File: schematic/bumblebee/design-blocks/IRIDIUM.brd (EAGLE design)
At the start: 3 parts

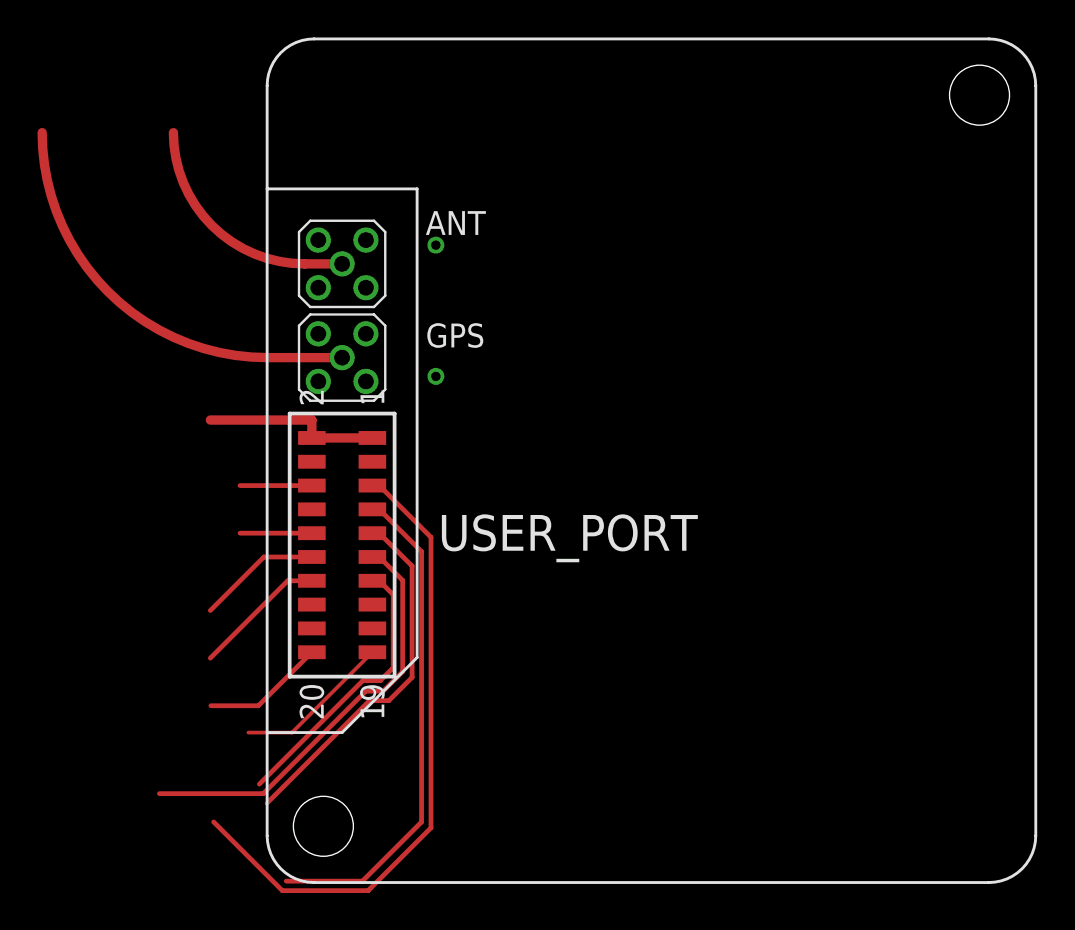
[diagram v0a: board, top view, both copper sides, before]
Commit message: Добавлена библиотека с разьёмами для игла Design-block иридиума Вроде готовая схема ICU, но её нужно проверить и причесать
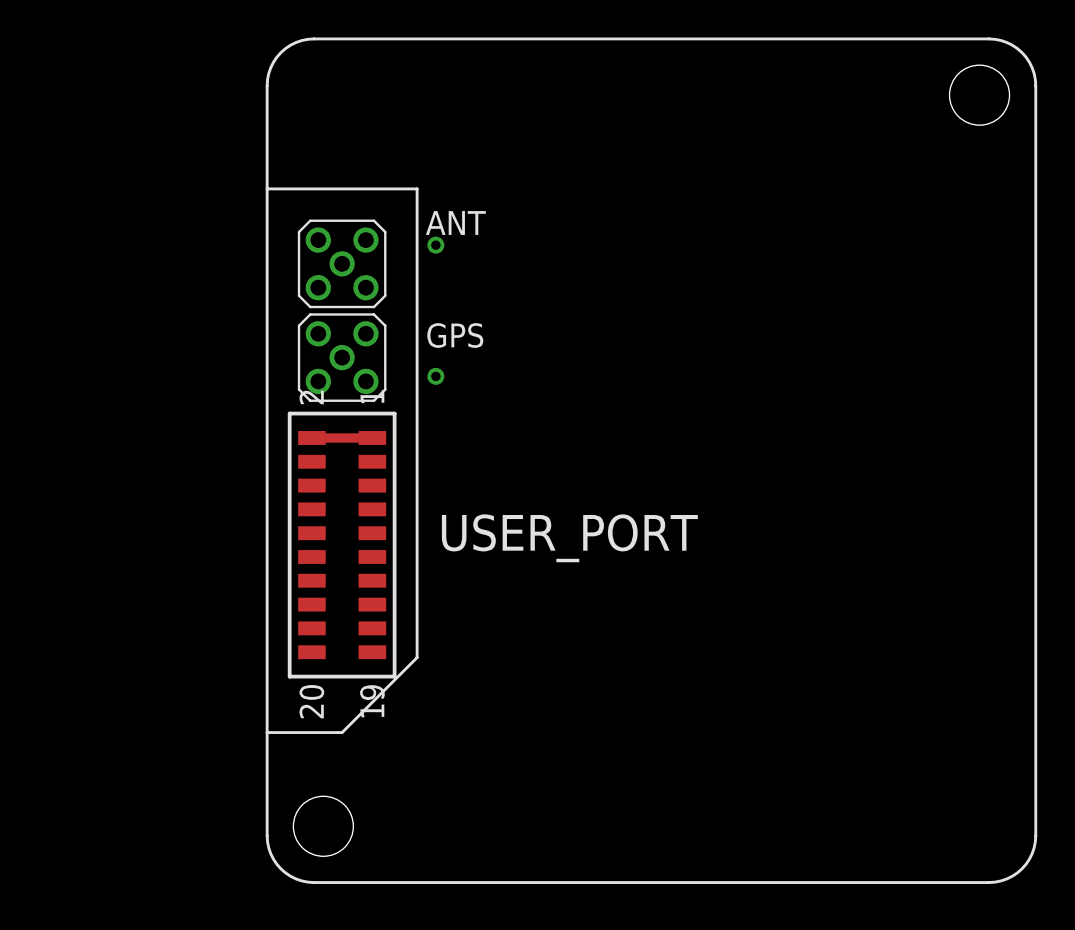
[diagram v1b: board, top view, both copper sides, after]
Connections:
- net DF_CTS renamed S$4
- net DF_DCD renamed S$3
- net DF_RTS renamed S$5
- net DF_S_RX renamed S$1
- net ON_OFF renamed S$2
- removed net DF_DSR: USER_PORT.10
- removed net DF_DTR: USER_PORT.14
- removed net DF_RI: USER_PORT.12
- removed net DF_S_TX: USER_PORT.6
- removed net N$21: ANT.1
- removed net N$22: GPS.1
- removed net NETWORK_AVAILABLE: USER_PORT.19
- removed net SUPPLY_OUT: USER_PORT.20
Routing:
- net S$2: track 34.3 -> 0.32 mm
- net S$1: track 26.5 -> 0.40 mm
- net S$4: track 22.7 -> 0.40 mm
- net N$22: track 21.0 -> 0.00 mm
- net S$3: track 19.4 -> 0.32 mm
- net S$5: track 15.0 -> 0.40 mm
- net N$21: track 11.9 -> 0.00 mm
- net NETWORK_AVAILABLE: track 8.39 -> 0.00 mm
- net DF_DTR: track 7.13 -> 0.00 mm
- net DF_RI: track 6.60 -> 0.00 mm
- net SUPPLY_OUT: track 6.57 -> 0.00 mm
- net VCC5: track 9.60 -> 3.23 mm
- net DF_S_TX: track 3.83 -> 0.00 mm
- net DF_DSR: track 3.83 -> 0.00 mm
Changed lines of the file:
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@@
 <via x="37.43" y="55.78" extent="1-16" drill="0.5"/>
-</signal>
-<signal name="NETWORK_AVAILABLE">
-<contactref element="USER_PORT" pad="19"/>
-<wire x1="34.043" y1="34.065" x2="29.758" y2="29.78" width="0.2" layer="1"/>
-<wire x1="29.758" y1="29.78" x2="27.43" y2="29.78" width="0.2" layer="1"/>
-</signal>
-<signal name="SUPPLY_OUT">
-<contactref element="USER_PORT" pad="20"/>
-<wire x1="30.817" y1="34.065" x2="27.962" y2="31.21" width="0.254" layer="1"/>
-<wire x1="27.962" y1="31.21" x2="25.43" y2="31.21" width="0.254" layer="1"/>
 </signal>
 <signal name="RESERVED_1">
 <contactref element="USER_PORT" pad="16"/>
 </signal>
-<signal name="DF_DTR">
-<contactref element="USER_PORT" pad="14"/>
-<wire x1="30.817" y1="37.875" x2="29.525" y2="37.875" width="0.254" layer="1"/>
-<wire x1="29.525" y1="37.875" x2="25.4" y2="33.75" width="0.254" layer="1"/>
-</signal>
-<signal name="DF_RI">
-<contactref element="USER_PORT" pad="12"/>
-<wire x1="30.817" y1="39.145" x2="28.255" y2="39.145" width="0.254" layer="1"/>
-<wire x1="28.255" y1="39.145" x2="25.4" y2="36.29" width="0.254" layer="1"/>
-</signal>
-<signal name="DF_DSR">
-<contactref element="USER_PORT" pad="10"/>
-<wire x1="30.817" y1="40.415" x2="26.985" y2="40.415" width="0.254" layer="1"/>
-</signal>
-<signal name="DF_S_TX">
-<contactref element="USER_PORT" pad="6"/>
-<wire x1="30.817" y1="42.955" x2="26.985" y2="42.955" width="0.254" layer="1"/>
-</signal>
 <signal name="RESERVED_2\">
 <contactref element="USER_PORT" pad="17"/>
 </signal>
-<signal name="DF_RTS">
+<signal name="S$5">
 <contactref element="USER_PORT" pad="13"/>
-<wire x1="34.43415625" y1="37.852" x2="35.155" y2="37.13115625" width="0.254" layer="1"/>
 <wire x1="34.043" y1="37.875" x2="34.066" y2="37.852" width="0.254" layer="1"/>
 <wire x1="34.066" y1="37.852" x2="34.43415625" y2="37.852" width="0.254" layer="1"/>
-<wire x1="35.155" y1="37.13115625" x2="35.155" y2="33.23884375" width="0.254" layer="1"/>
-<wire x1="35.155" y1="33.23884375" x2="34.463078125" y2="32.546921875" width="0.254" layer="1"/>
-<wire x1="34.463078125" y1="32.546921875" x2="33.532921875" y2="32.546921875" width="0.254" layer="1"/>
-<wire x1="33.532921875" y1="32.546921875" x2="28.013" y2="27.027" width="0.254" layer="1"/>
-<wire x1="22.89220625" y1="27.027" x2="28.013" y2="27.027" width="0" layer="19" extent="1-1"/>
 </signal>
-<signal name="DF_CTS">
+<signal name="S$4">
 <contactref element="USER_PORT" pad="11"/>
-<wire x1="28.22176875" y1="26.523" x2="22.6834375" y2="26.523" width="0.254" layer="1"/>
-<wire x1="35.659" y1="33.030075" x2="34.6194625" y2="31.9905375" width="0.254" layer="1"/>
 <wire x1="34.043" y1="39.145" x2="34.066" y2="39.122" width="0.254" layer="1"/>
 <wire x1="34.066" y1="39.122" x2="34.43415625" y2="39.122" width="0.254" layer="1"/>
-<wire x1="34.43415625" y1="39.122" x2="35.659" y2="37.89715625" width="0.254" layer="1"/>
-<wire x1="35.659" y1="37.89715625" x2="35.659" y2="33.030075" width="0.254" layer="1"/>
-<wire x1="34.6194625" y1="31.9905375" x2="33.68930625" y2="31.9905375" width="0.254" layer="1"/>
-<wire x1="33.68930625" y1="31.9905375" x2="28.22176875" y2="26.523" width="0.254" layer="1"/>
 </signal>
-<signal name="DF_DCD">
+<signal name="S$3">
 <contactref element="USER_PORT" pad="9"/>
-<wire x1="36.163" y1="32.72130625" x2="34.925846875" y2="31.484153125" width="0.254" layer="1"/>
+<wire x1="34.043" y1="40.415" x2="34.089" y2="40.415" width="0.254" layer="1"/>
 <wire x1="34.166" y1="40.492" x2="34.089" y2="40.415" width="0.254" layer="1"/>
-<wire x1="34.043" y1="40.415" x2="34.089" y2="40.415" width="0.254" layer="1"/>
 <wire x1="34.166" y1="40.492" x2="34.33415625" y2="40.492" width="0.254" layer="1"/>
-<wire x1="34.33415625" y1="40.492" x2="36.163" y2="38.66315625" width="0.254" layer="1"/>
-<wire x1="36.163" y1="38.66315625" x2="36.163" y2="32.72130625" width="0.254" layer="1"/>
-<wire x1="34.925846875" y1="31.484153125" x2="33.895690625" y2="31.484153125" width="0.254" layer="1"/>
-<wire x1="33.895690625" y1="31.484153125" x2="28.4305375" y2="26.019" width="0.254" layer="1"/>
-<wire x1="28.4305375" y1="26.019" x2="22.47466875" y2="26.019" width="0" layer="19" extent="1-1"/>
 </signal>
-<signal name="DF_S_RX">
+<signal name="S$1">
 <contactref element="USER_PORT" pad="7"/>
-<wire x1="33.5110375" y1="21.853" x2="29.4489625" y2="21.853" width="0.254" layer="1"/>
 <wire x1="34.043" y1="41.685" x2="34.066" y2="41.662" width="0.254" layer="1"/>
 <wire x1="34.066" y1="41.662" x2="34.43415625" y2="41.662" width="0.254" layer="1"/>
-<wire x1="34.43415625" y1="41.662" x2="36.667" y2="39.42915625" width="0.254" layer="1"/>
-<wire x1="36.667" y1="39.42915625" x2="36.667" y2="25.0089625" width="0.254" layer="1"/>
-<wire x1="36.667" y1="25.0089625" x2="33.5110375" y2="21.853" width="0.254" layer="1"/>
-<wire x1="22.2659" y1="25.515" x2="29.4489625" y2="21.853" width="0" layer="19" extent="1-1"/>
 </signal>
-<signal name="ON_OFF">
+<signal name="S$2">
 <contactref element="USER_PORT" pad="5"/>
-<wire x1="37.171" y1="24.70019375" x2="33.81980625" y2="21.349" width="0.254" layer="1"/>
-<wire x1="33.81980625" y1="21.349" x2="29.24019375" y2="21.349" width="0.254" layer="1"/>
-<wire x1="29.24019375" y1="21.349" x2="25.57819375" y2="25.011" width="0.254" layer="1"/>
+<wire x1="34.043" y1="42.955" x2="34.12" y2="43.032" width="0.254" layer="1"/>
 <wire x1="34.33415625" y1="43.032" x2="34.12" y2="43.032" width="0.254" layer="1"/>
-<wire x1="34.043" y1="42.955" x2="34.12" y2="43.032" width="0.254" layer="1"/>
-<wire x1="34.33415625" y1="43.032" x2="37.171" y2="40.19515625" width="0.254" layer="1"/>
-<wire x1="37.171" y1="40.19515625" x2="37.171" y2="24.70019375" width="0.254" layer="1"/>
-</signal>
-<signal name="N$21" class="2">
-<contactref element="ANT" pad="1"/>
-<wire x1="32.43" y1="54.78" x2="30.43" y2="54.78" width="0.5" layer="1"/>
-<wire x1="30.43" y1="54.78" x2="23.43" y2="61.78" width="0.5" layer="1" curve="-90"/>
-</signal>
-<signal name="N$22" class="2">
-<contactref element="GPS" pad="1"/>
-<wire x1="16.43" y1="61.78" x2="28.43" y2="49.78" width="0.5" layer="1" curve="90"/>
-<wire x1="28.43" y1="49.78" x2="32.43" y2="49.78" width="0.5" layer="1"/>
 </signal>
 <signal name="VCC5" class="1">
@@
 <contactref element="USER_PORT" pad="1"/>
 <wire x1="34.043" y1="45.495" x2="30.817" y2="45.495" width="0.5" layer="1"/>
-<wire x1="25.4" y1="46.45" x2="30.817" y2="46.45" width="0.5" layer="1"/>
-<wire x1="30.817" y1="46.45" x2="30.817" y2="45.495" width="0.5" layer="1"/>
 </signal>
 </signals>
